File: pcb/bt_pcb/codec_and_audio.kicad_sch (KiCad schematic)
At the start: 20 parts, among them IC2 ADAU1961WBCPZ-R7, J4 Conn_01x01, J5 Conn_01x03

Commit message: first reiteration
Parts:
- J5: footprint Connector_PinHeader_2.54mm:PinHeader_1x03_P2.54mm_Vertical -> Connector_JST:JST_PH_B3B-PH-K_1x03_P2.00mm_Vertical
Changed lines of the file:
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@@
 			)
 		)
-		(property "Footprint" "Connector_PinHeader_2.54mm:PinHeader_1x03_P2.54mm_Vertical"
+		(property "Footprint" "Connector_JST:JST_PH_B3B-PH-K_1x03_P2.00mm_Vertical"
 			(at 259.08 135.89 0)
 			(effects

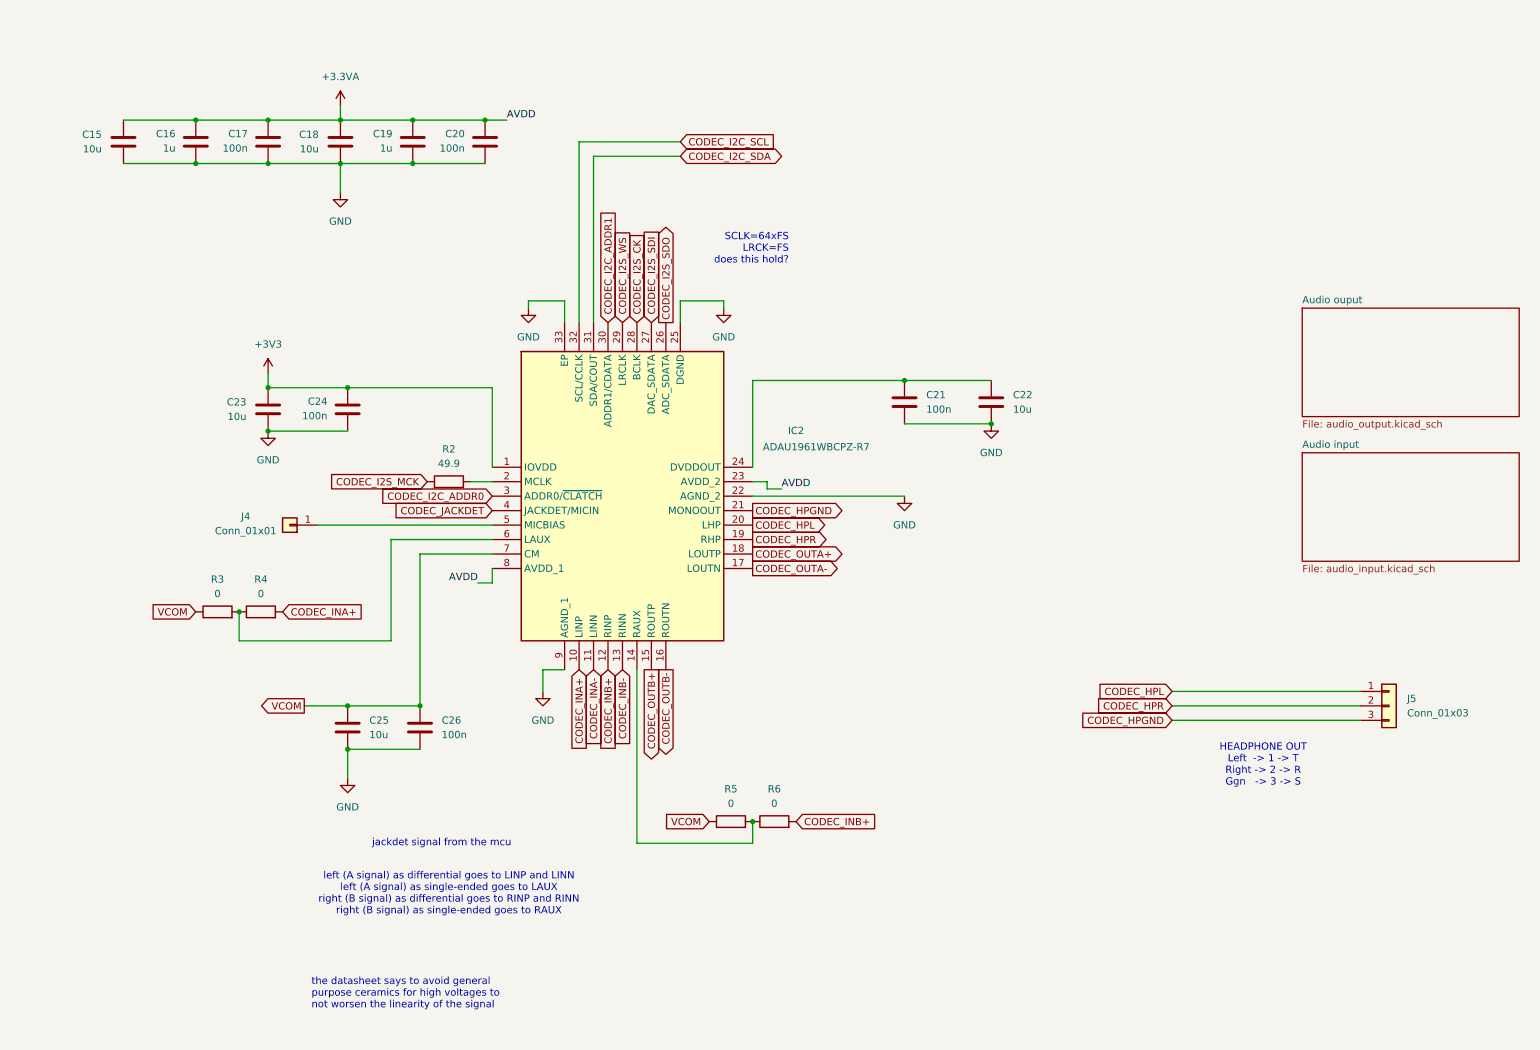
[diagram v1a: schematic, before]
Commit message: redo of power supply
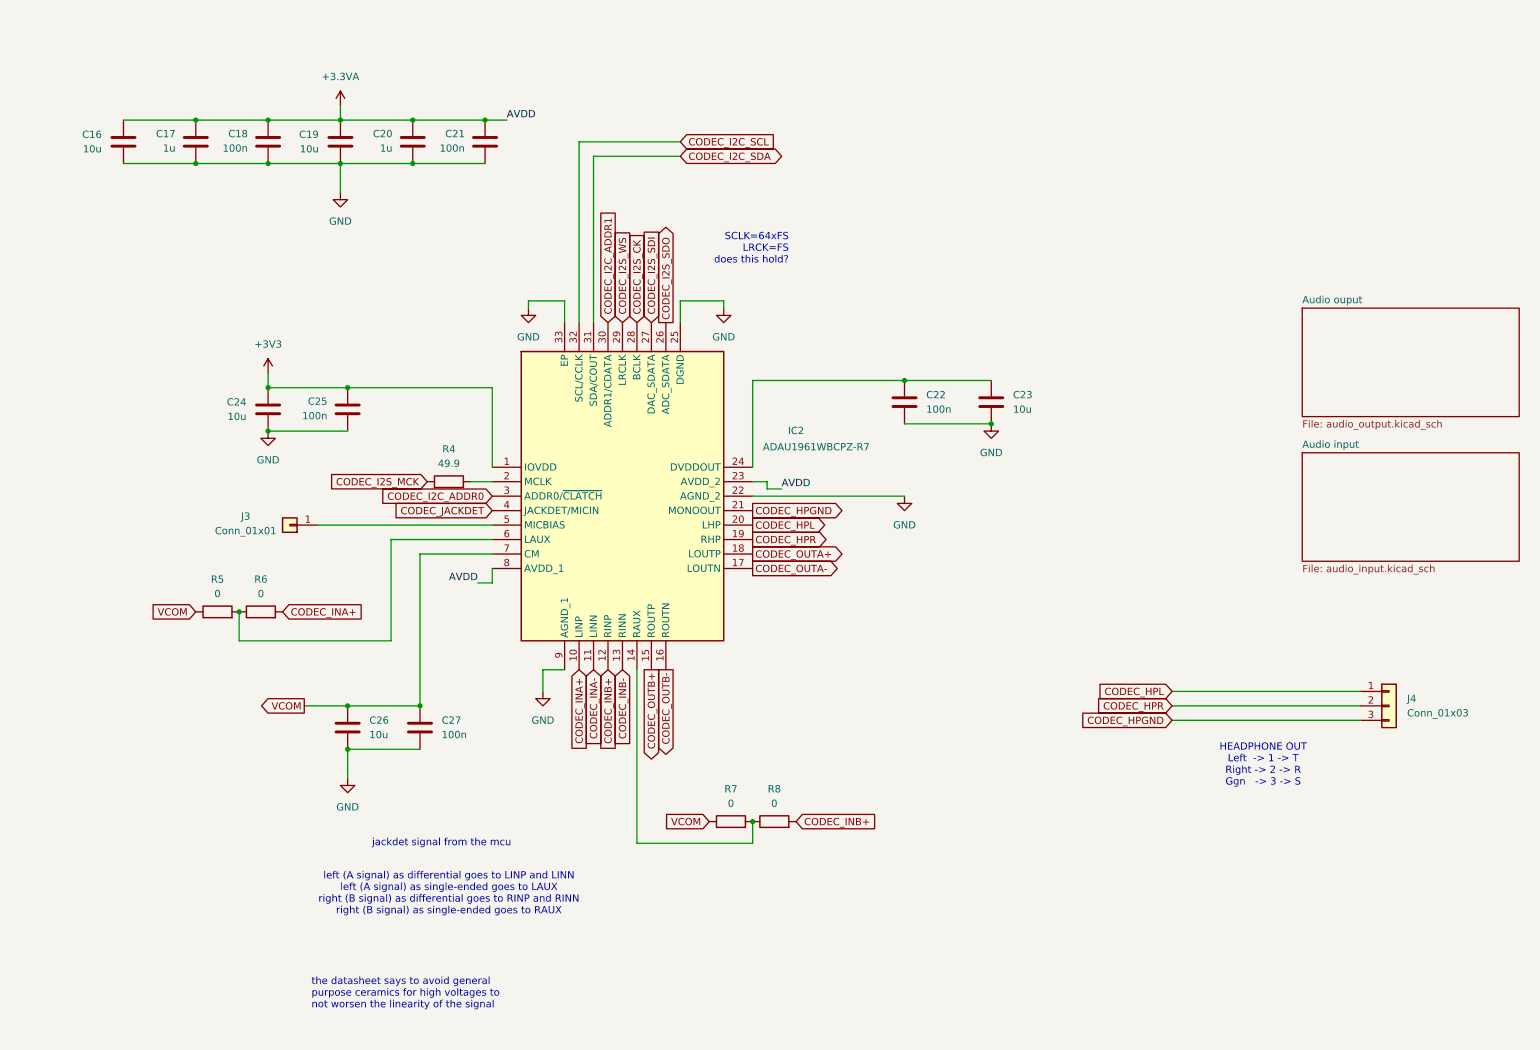
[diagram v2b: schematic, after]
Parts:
- renumbered C15 to C16, C16 to C17, C17 to C18, C18 to C19, C19 to C20, C20 to C21, C21 to C22, C22 to C23, C23 to C24, C24 to C25, C25 to C26, C26 to C27, J4 to J3, J5 to J4, R2 to R4, R3 to R5, R4 to R6, R5 to R7, R6 to R8
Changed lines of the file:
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@@
 		(dnp no)
 		(fields_autoplaced yes)
-		(property "Reference" "#PWR025"
+		(property "Reference" "#PWR027"
 			(at 62.23 81.28 0)
 			(effects
@@
 			(project ""
 				(path "/eb787481-08cd-41a4-a128-173fa6227c32/4ada0139-8712-47ce-9d4c-ab8fef312f7b"
-					(reference "#PWR025")
+					(reference "#PWR027")
 					(unit 1)
 				)
@@
 		(on_board yes)
 		(dnp no)
-		(property "Reference" "C24"
+		(property "Reference" "C25"
 			(at 72.644 82.423 0)
 			(effects
@@
 			(project "bt_pcb"
 				(path "/eb787481-08cd-41a4-a128-173fa6227c32/4ada0139-8712-47ce-9d4c-ab8fef312f7b"
-					(reference "C24")
+					(reference "C25")
 					(unit 1)
 				)
@@
 		(dnp no)
 		(fields_autoplaced yes)
-		(property "Reference" "#PWR023"
+		(property "Reference" "#PWR025"
 			(at 107.95 72.39 0)
 			(effects
@@
 			(project "bt_pcb"
 				(path "/eb787481-08cd-41a4-a128-173fa6227c32/4ada0139-8712-47ce-9d4c-ab8fef312f7b"
-					(reference "#PWR023")
+					(reference "#PWR025")
 					(unit 1)
 				)
@@
 		(dnp no)
 		(fields_autoplaced yes)
-		(property "Reference" "R3"
+		(property "Reference" "R5"
 			(at 53.34 113.665 90)
 			(effects
@@
 			(project "bt_pcb"
 				(path "/eb787481-08cd-41a4-a128-173fa6227c32/4ada0139-8712-47ce-9d4c-ab8fef312f7b"
-					(reference "R3")
+					(reference "R5")
 					(unit 1)
 				)
@@
 		(dnp no)
 		(fields_autoplaced yes)
-		(property "Reference" "R5"
+		(property "Reference" "R7"
 			(at 143.51 150.495 90)
 			(effects
@@
 			(project "bt_pcb"
 				(path "/eb787481-08cd-41a4-a128-173fa6227c32/4ada0139-8712-47ce-9d4c-ab8fef312f7b"
-					(reference "R5")
+					(reference "R7")
 					(unit 1)
 				)
@@
 		(dnp no)
 		(fields_autoplaced yes)
-		(property "Reference" "#PWR026"
+		(property "Reference" "#PWR028"
 			(at 189.23 92.71 0)
 			(effects
@@
 			(project "bt_pcb"
 				(path "/eb787481-08cd-41a4-a128-173fa6227c32/4ada0139-8712-47ce-9d4c-ab8fef312f7b"
-					(reference "#PWR026")
+					(reference "#PWR028")
 					(unit 1)
 				)
@@
 		(on_board yes)
 		(dnp no)
-		(property "Reference" "C23"
+		(property "Reference" "C24"
 			(at 58.42 82.55 0)
 			(effects
@@
 			(project "bt_pcb"
 				(path "/eb787481-08cd-41a4-a128-173fa6227c32/4ada0139-8712-47ce-9d4c-ab8fef312f7b"
-					(reference "C23")
+					(reference "C24")
 					(unit 1)
 				)
@@
 		(dnp no)
 		(fields_autoplaced yes)
-		(property "Reference" "#PWR029"
+		(property "Reference" "#PWR031"
 			(at 110.49 139.7 0)
 			(effects
@@
 			(project "bt_pcb"
 				(path "/eb787481-08cd-41a4-a128-173fa6227c32/4ada0139-8712-47ce-9d4c-ab8fef312f7b"
-					(reference "#PWR029")
+					(reference "#PWR031")
 					(unit 1)
 				)
@@
 		(dnp no)
 		(fields_autoplaced yes)
-		(property "Reference" "R2"
+		(property "Reference" "R4"
 			(at 93.98 90.805 90)
 			(effects
@@
 			(project ""
 				(path "/eb787481-08cd-41a4-a128-173fa6227c32/4ada0139-8712-47ce-9d4c-ab8fef312f7b"
-					(reference "R2")
+					(reference "R4")
 					(unit 1)
 				)
@@
 		(dnp no)
 		(fields_autoplaced yes)
-		(property "Reference" "#PWR027"
+		(property "Reference" "#PWR029"
 			(at 62.23 93.98 0)
 			(effects
@@
 			(project "bt_pcb"
 				(path "/eb787481-08cd-41a4-a128-173fa6227c32/4ada0139-8712-47ce-9d4c-ab8fef312f7b"
-					(reference "#PWR027")
+					(reference "#PWR029")
 					(unit 1)
 				)
@@
 		(on_board yes)
 		(dnp no)
-		(property "Reference" "C19"
+		(property "Reference" "C20"
 			(at 84.074 35.433 0)
 			(effects
@@
 			(project "bt_pcb"
 				(path "/eb787481-08cd-41a4-a128-173fa6227c32/4ada0139-8712-47ce-9d4c-ab8fef312f7b"
-					(reference "C19")
+					(reference "C20")
 					(unit 1)
 				)
@@
 		(on_board yes)
 		(dnp no)
-		(property "Reference" "C22"
+		(property "Reference" "C23"
 			(at 193.04 81.28 0)
 			(effects
@@
 			(project "bt_pcb"
 				(path "/eb787481-08cd-41a4-a128-173fa6227c32/4ada0139-8712-47ce-9d4c-ab8fef312f7b"
-					(reference "C22")
+					(reference "C23")
 					(unit 1)
 				)
@@
 		(on_board yes)
 		(dnp no)
-		(property "Reference" "C25"
+		(property "Reference" "C26"
 			(at 80.01 138.43 0)
 			(effects
@@
 			(project "bt_pcb"
 				(path "/eb787481-08cd-41a4-a128-173fa6227c32/4ada0139-8712-47ce-9d4c-ab8fef312f7b"
-					(reference "C25")
+					(reference "C26")
 					(unit 1)
 				)
@@
 		(on_board yes)
 		(dnp no)
-		(property "Reference" "C17"
+		(property "Reference" "C18"
 			(at 58.674 35.433 0)
 			(effects
@@
 			(project "bt_pcb"
 				(path "/eb787481-08cd-41a4-a128-173fa6227c32/4ada0139-8712-47ce-9d4c-ab8fef312f7b"
-					(reference "C17")
+					(reference "C18")
 					(unit 1)
 				)
@@
 		(dnp no)
 		(fields_autoplaced yes)
-		(property "Reference" "#PWR021"
+		(property "Reference" "#PWR023"
 			(at 74.93 34.29 0)
 			(effects
@@
 			(project ""
 				(path "/eb787481-08cd-41a4-a128-173fa6227c32/4ada0139-8712-47ce-9d4c-ab8fef312f7b"
-					(reference "#PWR021")
+					(reference "#PWR023")
 					(unit 1)
 				)
@@
 		(dnp no)
 		(fields_autoplaced yes)
-		(property "Reference" "#PWR030"
+		(property "Reference" "#PWR032"
 			(at 76.2 154.94 0)
 			(effects
@@
 			(project "bt_pcb"
 				(path "/eb787481-08cd-41a4-a128-173fa6227c32/4ada0139-8712-47ce-9d4c-ab8fef312f7b"
-					(reference "#PWR030")
+					(reference "#PWR032")
 					(unit 1)
 				)
@@
 		(dnp no)
 		(fields_autoplaced yes)
-		(property "Reference" "J5"
+		(property "Reference" "J4"
 			(at 262.255 134.6199 0)
 			(effects
@@
 			(project "bt_pcb"
 				(path "/eb787481-08cd-41a4-a128-173fa6227c32/4ada0139-8712-47ce-9d4c-ab8fef312f7b"
-					(reference "J5")
+					(reference "J4")
 					(unit 1)
 				)
@@
 		(dnp no)
 		(fields_autoplaced yes)
-		(property "Reference" "R6"
+		(property "Reference" "R8"
 			(at 151.13 150.495 90)
 			(effects
@@
 			(project "bt_pcb"
 				(path "/eb787481-08cd-41a4-a128-173fa6227c32/4ada0139-8712-47ce-9d4c-ab8fef312f7b"
-					(reference "R6")
+					(reference "R8")
 					(unit 1)
 				)
@@
 		(dnp no)
 		(fields_autoplaced yes)
-		(property "Reference" "R4"
+		(property "Reference" "R6"
 			(at 60.96 113.665 90)
 			(effects
@@
 			(project "bt_pcb"
 				(path "/eb787481-08cd-41a4-a128-173fa6227c32/4ada0139-8712-47ce-9d4c-ab8fef312f7b"
-					(reference "R4")
+					(reference "R6")
 					(unit 1)
 				)
@@
 		(on_board yes)
 		(dnp no)
-		(property "Reference" "C26"
+		(property "Reference" "C27"
 			(at 92.71 138.43 0)
 			(effects
@@
 			(project "bt_pcb"
 				(path "/eb787481-08cd-41a4-a128-173fa6227c32/4ada0139-8712-47ce-9d4c-ab8fef312f7b"
-					(reference "C26")
+					(reference "C27")
 					(unit 1)
 				)
@@
 		(dnp no)
 		(fields_autoplaced yes)
-		(property "Reference" "#PWR022"
+		(property "Reference" "#PWR024"
 			(at 74.93 52.07 0)
 			(effects
@@
 			(project "bt_pcb"
 				(path "/eb787481-08cd-41a4-a128-173fa6227c32/4ada0139-8712-47ce-9d4c-ab8fef312f7b"
-					(reference "#PWR022")
+					(reference "#PWR024")
 					(unit 1)
 				)
@@
 		(on_board yes)
 		(dnp no)
-		(property "Reference" "C20"
+		(property "Reference" "C21"
 			(at 96.774 35.433 0)
 			(effects
@@
 			(project "bt_pcb"
 				(path "/eb787481-08cd-41a4-a128-173fa6227c32/4ada0139-8712-47ce-9d4c-ab8fef312f7b"
-					(reference "C20")
+					(reference "C21")
 					(unit 1)
 				)
@@
 		(on_board yes)
 		(dnp no)
-		(property "Reference" "C18"
+		(property "Reference" "C19"
 			(at 71.12 35.56 0)
 			(effects
@@
 			(project "bt_pcb"
 				(path "/eb787481-08cd-41a4-a128-173fa6227c32/4ada0139-8712-47ce-9d4c-ab8fef312f7b"
-					(reference "C18")
+					(reference "C19")
 					(unit 1)
 				)
@@
 		(on_board yes)
 		(dnp no)
-		(property "Reference" "J4"
+		(property "Reference" "J3"
 			(at 58.293 102.616 0)
 			(effects
@@
 			(project "bt_pcb"
 				(path "/eb787481-08cd-41a4-a128-173fa6227c32/4ada0139-8712-47ce-9d4c-ab8fef312f7b"
-					(reference "J4")
+					(reference "J3")
 					(unit 1)
 				)
@@
 		(on_board yes)
 		(dnp no)
-		(property "Reference" "C15"
+		(property "Reference" "C16"
 			(at 33.02 35.56 0)
 			(effects
@@
 			(project "bt_pcb"
 				(path "/eb787481-08cd-41a4-a128-173fa6227c32/4ada0139-8712-47ce-9d4c-ab8fef312f7b"
-					(reference "C15")
+					(reference "C16")
 					(unit 1)
 				)
@@
 		(on_board yes)
 		(dnp no)
-		(property "Reference" "C21"
+		(property "Reference" "C22"
 			(at 177.8 81.28 0)
 			(effects
@@
 			(project "bt_pcb"
 				(path "/eb787481-08cd-41a4-a128-173fa6227c32/4ada0139-8712-47ce-9d4c-ab8fef312f7b"
-					(reference "C21")
+					(reference "C22")
 					(unit 1)
 				)
@@
 		(dnp no)
 		(fields_autoplaced yes)
-		(property "Reference" "#PWR024"
+		(property "Reference" "#PWR026"
 			(at 142.24 72.39 0)
 			(effects
@@
 			(project "bt_pcb"
 				(path "/eb787481-08cd-41a4-a128-173fa6227c32/4ada0139-8712-47ce-9d4c-ab8fef312f7b"
-					(reference "#PWR024")
+					(reference "#PWR026")
 					(unit 1)
 				)
@@
 		(on_board yes)
 		(dnp no)
-		(property "Reference" "C16"
+		(property "Reference" "C17"
 			(at 45.974 35.433 0)
 			(effects
@@
 			(project "bt_pcb"
 				(path "/eb787481-08cd-41a4-a128-173fa6227c32/4ada0139-8712-47ce-9d4c-ab8fef312f7b"
-					(reference "C16")
+					(reference "C17")
 					(unit 1)
 				)
@@
 		(dnp no)
 		(fields_autoplaced yes)
-		(property "Reference" "#PWR028"
+		(property "Reference" "#PWR030"
 			(at 173.99 105.41 0)
 			(effects
@@
 			(project "bt_pcb"
 				(path "/eb787481-08cd-41a4-a128-173fa6227c32/4ada0139-8712-47ce-9d4c-ab8fef312f7b"
-					(reference "#PWR028")
-					(unit 1)
-				)
+					(reference "#PWR030")
+					(unit 1)
+				)
